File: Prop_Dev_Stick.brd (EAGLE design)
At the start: 63.2 x 24.9 mm, 54 parts, among them J1 MF-CON-MICROUSB-RIGHT, J3 M20-7822046, J4 M20-7822046, J5 M20-7820442, J6 M20-7820442, U1 P8X32A-Q44, U2 FT230XQ-R, U3 TPS2113ADRBR, U4 CAT24C512WI-GT3, U5 AD7999YRJZ-1500RL7, U6 TS2937CW33, U7 IRLML6401TRPBF, X1 ATS060CSM-1

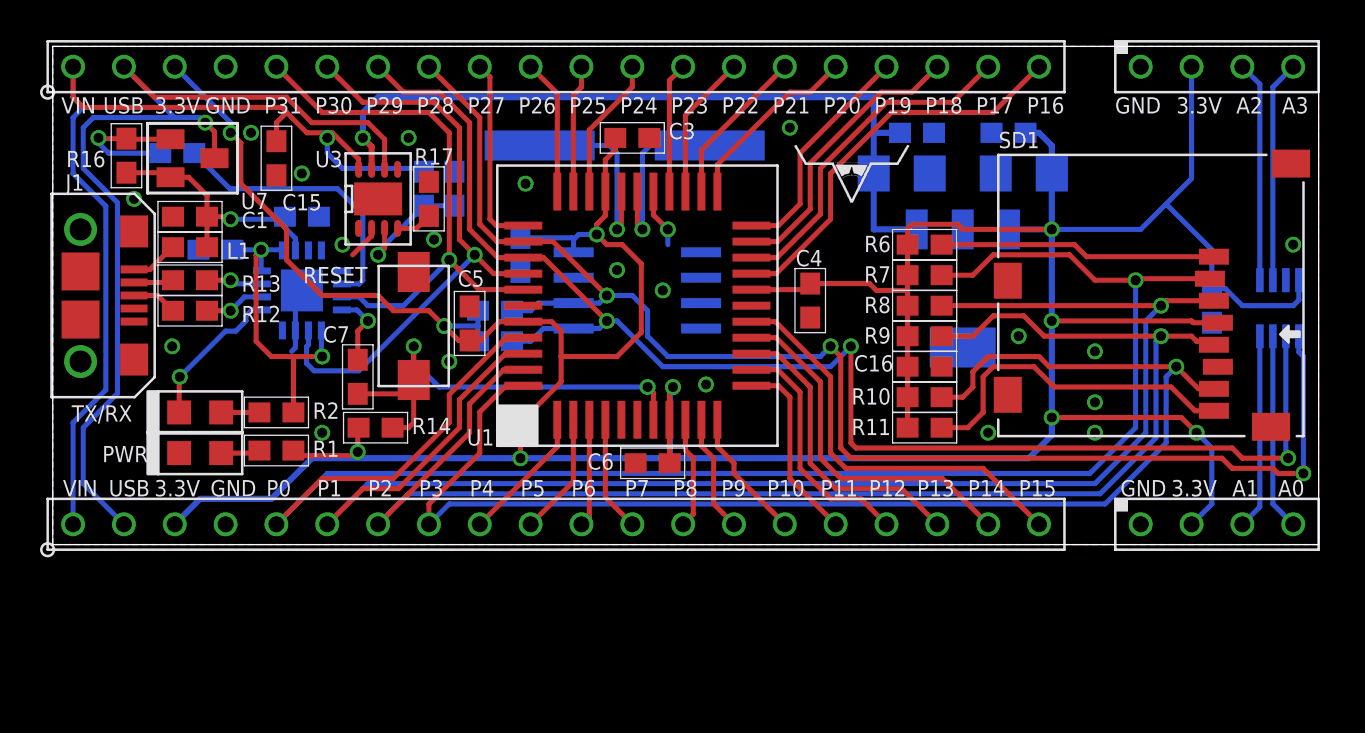
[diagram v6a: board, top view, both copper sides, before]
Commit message: Changed crystal.
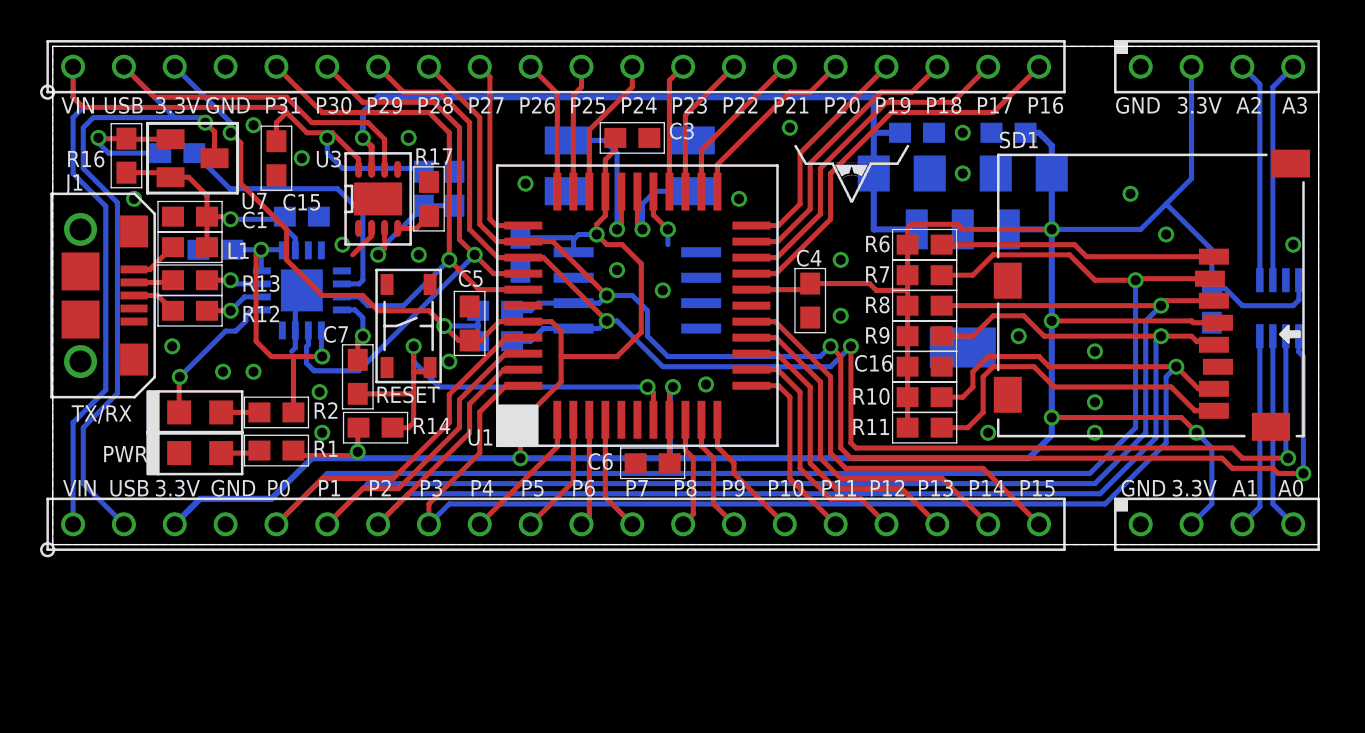
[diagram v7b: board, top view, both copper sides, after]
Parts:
- RESET: value 101-0134-EV -> MF-SW-TACT-4.2MM; device PP_Electromechanical:101-0134-EV -> MF_Switches:TACT4.2MM
- X1: value ATS060CSM-1 -> ABMM-6.000MHZ-B2-T; device PP_FreqCtrl:HC-49/US_SM -> MF_Frequency_Control:7MMX5MM
- moved X1 1.05 mm to (28.8, 18.9), turned to 0 degrees
- moved RESET 0.25 mm to (17.8, 10.9)
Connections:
- net GND: now also RESET.P$3, RESET.P$4, X1.P$2, X1.P$4; no longer RESET.1
- net RES: now also RESET.P$2; no longer RESET.2
- net X0: now also X1.P$3; no longer X1.P$1
- net X1: now also X1.P$1; no longer X1.P$2
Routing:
- net X1: track 9.32 -> 6.04 mm
- net X0: track 9.82 -> 8.57 mm
- net RES: track 22.8 -> 23.5 mm
- net GND: vias 21 -> 31
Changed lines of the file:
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@@
 <attribute name="DRAWING_NAME" x="62.738" y="19.05" size="0.8128" layer="22" font="vector" rot="MR0"/>
-</element>
-<element name="X1" library="PP_FreqCtrl" package="HC-49/US_SM" value="ATS060CSM-1" x="28.575" y="19.939" smashed="yes" rot="MR180">
-<attribute name="NAME" x="34.417" y="18.415" size="0.8128" layer="22" font="vector" rot="MR180"/>
 </element>
 <element name="U2" library="PP_DigitalIC" package="QFN-16" value="FT230XQ-R" x="12.446" y="12.7" smashed="yes" rot="MR90">
@@
 <element name="C7" library="PP_Passives" package="0603" value=".1uF" x="15.24" y="8.382" smashed="yes" rot="R270">
 <attribute name="NAME" x="13.497" y="10.0965" size="0.8128" layer="25" font="vector"/>
-</element>
-<element name="RESET" library="PP_Electromechanical" package="101-0134-EV" value="101-0134-EV" x="18.034" y="10.922" smashed="yes" rot="R270">
-<attribute name="NAME" x="12.51" y="13.057" size="0.8128" layer="25" font="vector"/>
 </element>
 <element name="U4" library="PP_DigitalIC" package="SOIC-8_W" value="CAT24C512WI-GT3" x="29.21" y="12.7" smashed="yes" rot="MR270">
@@
 <element name="J1" library="MF_Connectors" package="MICROUSB-RIGHT" value="MF-CON-MICROUSB-RIGHT" x="2.794" y="12.446" smashed="yes" rot="R270">
 <attribute name="NAME" x="0.635" y="17.686" size="0.8128" layer="25" font="vector"/>
+</element>
+<element name="X1" library="MF_Frequency_Control" package="7MMX5MM" value="ABMM-6.000MHZ-B2-T" x="28.829" y="18.923" smashed="yes" rot="MR0">
+<attribute name="NAME" x="32.429" y="21.923" size="0.8128" layer="26" font="vector" rot="MR0"/>
+</element>
+<element name="RESET" library="MF_Switches" package="TACT4.2MM" value="MF-SW-TACT-4.2MM" x="17.78" y="10.922" smashed="yes" rot="R270">
+<attribute name="NAME" x="16.123" y="7.08" size="0.8128" layer="25" font="vector"/>
 </element>
 </elements>
@@
 <contactref element="C4" pad="1"/>
 <contactref element="C5" pad="1"/>
-<contactref element="RESET" pad="1"/>
 <contactref element="U4" pad="4"/>
 <contactref element="U4" pad="2"/>
@@
 <via x="17.78" y="20.32" extent="1-16" drill="0.5"/>
 <via x="14.478" y="14.986" extent="1-16" drill="0.5"/>
-<via x="9.906" y="20.574" extent="1-16" drill="0.5"/>
+<via x="10.033" y="20.955" extent="1-16" drill="0.5"/>
 <via x="13.462" y="5.588" extent="1-16" drill="0.5"/>
 <wire x1="12.121" y1="10.7" x2="12.121" y2="9.835" width="0.254" layer="16"/>
 <wire x1="12.121" y1="9.835" x2="11.938" y2="9.652" width="0.254" layer="16"/>
 <wire x1="12.121" y1="12.375" x2="12.121" y2="10.7" width="0.254" layer="16"/>
-<via x="12.446" y="18.542" extent="1-16" drill="0.5"/>
+<via x="12.446" y="19.304" extent="1-16" drill="0.5"/>
 <via x="46.736" y="5.588" extent="1-16" drill="0.5"/>
 <via x="61.976" y="14.986" extent="1-16" drill="0.5"/>
@@
 <contactref element="J1" pad="S3"/>
 <contactref element="J1" pad="S2"/>
-<via x="19.05" y="15.24" extent="1-16" drill="0.5"/>
+<via x="18.288" y="14.478" extent="1-16" drill="0.5"/>
 <via x="23.622" y="18.034" extent="1-16" drill="0.5"/>
 <via x="28.194" y="13.716" extent="1-16" drill="0.5"/>
@@
 <wire x1="15.931" y1="15.797" x2="15.931" y2="15.423" width="0.254" layer="1"/>
 <wire x1="15.931" y1="15.423" x2="14.986" y2="14.478" width="0.254" layer="1"/>
+<contactref element="X1" pad="P$4"/>
+<contactref element="X1" pad="P$2"/>
+<contactref element="RESET" pad="P$3"/>
+<contactref element="RESET" pad="P$4"/>
+<via x="13.335" y="7.62" extent="1-16" drill="0.5"/>
+<via x="39.37" y="14.224" extent="1-16" drill="0.5"/>
+<via x="39.37" y="11.43" extent="1-16" drill="0.5"/>
+<via x="34.29" y="17.272" extent="1-16" drill="0.5"/>
+<via x="45.466" y="20.574" extent="1-16" drill="0.5"/>
+<via x="45.466" y="18.542" extent="1-16" drill="0.5"/>
+<via x="53.848" y="17.526" extent="1-16" drill="0.5"/>
+<via x="55.626" y="15.494" extent="1-16" drill="0.5"/>
+<via x="8.509" y="8.636" extent="1-16" drill="0.5"/>
+<via x="10.033" y="8.636" extent="1-16" drill="0.5"/>
 </signal>
 <signal name="SDA">
@@
 <signal name="RES">
 <contactref element="U1" pad="7"/>
-<contactref element="RESET" pad="2"/>
 <contactref element="R14" pad="1"/>
 <contactref element="C7" pad="2"/>
@@
 <wire x1="18.034" y1="9.144" x2="18.034" y2="9.906" width="0.254" layer="16"/>
 <via x="18.034" y="9.906" extent="1-16" drill="0.5"/>
-<wire x1="18.034" y1="9.906" x2="18.034" y2="8.222" width="0.254" layer="1"/>
-<wire x1="18.034" y1="8.222" x2="17.344" y2="7.532" width="0.254" layer="1"/>
-<wire x1="17.344" y1="7.532" x2="15.24" y2="7.532" width="0.254" layer="1"/>
+<wire x1="18.034" y1="7.532" x2="15.24" y2="7.532" width="0.254" layer="1"/>
 <wire x1="16.979" y1="5.842" x2="17.78" y2="5.842" width="0.254" layer="1"/>
 <wire x1="17.78" y1="5.842" x2="18.034" y2="6.096" width="0.254" layer="1"/>
-<wire x1="18.034" y1="6.096" x2="18.034" y2="8.222" width="0.254" layer="1"/>
+<contactref element="RESET" pad="P$2"/>
+<wire x1="18.034" y1="8.636" x2="18.034" y2="9.906" width="0.254" layer="1"/>
+<wire x1="18.855" y1="8.847" x2="18.812" y2="8.636" width="0.254" layer="1"/>
+<wire x1="18.812" y1="8.636" x2="18.034" y2="8.636" width="0.254" layer="1"/>
+<wire x1="18.034" y1="6.096" x2="18.034" y2="7.532" width="0.254" layer="1"/>
+<wire x1="18.034" y1="7.532" x2="18.034" y2="8.636" width="0.254" layer="1"/>
 </signal>
 <signal name="3.3V">
@@
 <wire x1="11.684" y1="15.748" x2="11.684" y2="14.224" width="0.254" layer="1"/>
 <wire x1="11.684" y1="14.224" x2="13.462" y2="12.446" width="0.254" layer="1"/>
-<wire x1="13.462" y1="12.446" x2="16.256" y2="12.446" width="0.254" layer="1"/>
-<wire x1="16.256" y1="12.446" x2="17.018" y2="11.684" width="0.254" layer="1"/>
-<wire x1="17.018" y1="11.684" x2="18.796" y2="11.684" width="0.254" layer="1"/>
+<wire x1="13.462" y1="12.446" x2="15.494" y2="12.446" width="0.254" layer="1"/>
+<wire x1="15.494" y1="12.446" x2="16.256" y2="11.684" width="0.254" layer="1"/>
+<wire x1="16.256" y1="11.684" x2="18.796" y2="11.684" width="0.254" layer="1"/>
 <wire x1="18.796" y1="11.684" x2="19.558" y2="10.922" width="0.254" layer="1"/>
 <wire x1="57.912" y1="12.788" x2="57.912" y2="14.732" width="0.254" layer="16"/>
@@
 <signal name="X0">
 <contactref element="U1" pad="29"/>
-<contactref element="X1" pad="P$1"/>
 <wire x1="28.41" y1="17.638" x2="28.41" y2="15.964" width="0.254" layer="1"/>
 <wire x1="28.41" y1="15.964" x2="28.194" y2="15.748" width="0.254" layer="1"/>
 <via x="28.194" y="15.748" extent="1-16" drill="0.5"/>
 <wire x1="28.194" y1="15.748" x2="28.194" y2="19.558" width="0.254" layer="16"/>
-<wire x1="28.194" y1="19.558" x2="27.813" y2="19.939" width="0.254" layer="16"/>
-<wire x1="27.813" y1="19.939" x2="24.325" y2="19.939" width="0.254" layer="16"/>
+<wire x1="28.194" y1="19.558" x2="27.559" y2="20.193" width="0.254" layer="16"/>
+<contactref element="X1" pad="P$3"/>
+<wire x1="27.559" y1="20.193" x2="25.679" y2="20.193" width="0.254" layer="16"/>
 </signal>
 <signal name="X1">
 <contactref element="U1" pad="28"/>
-<contactref element="X1" pad="P$2"/>
 <wire x1="29.21" y1="17.638" x2="29.21" y2="16.002" width="0.254" layer="1"/>
 <wire x1="29.21" y1="16.002" x2="29.464" y2="15.748" width="0.254" layer="1"/>
 <via x="29.464" y="15.748" extent="1-16" drill="0.5"/>
-<wire x1="29.464" y1="15.748" x2="29.464" y2="19.558" width="0.254" layer="16"/>
-<wire x1="29.464" y1="19.558" x2="29.845" y2="19.939" width="0.254" layer="16"/>
-<wire x1="29.845" y1="19.939" x2="32.825" y2="19.939" width="0.254" layer="16"/>
+<contactref element="X1" pad="P$1"/>
+<wire x1="29.464" y1="15.748" x2="29.464" y2="17.018" width="0.254" layer="16"/>
+<wire x1="29.464" y1="17.018" x2="30.099" y2="17.653" width="0.254" layer="16"/>
+<wire x1="30.099" y1="17.653" x2="31.979" y2="17.653" width="0.254" layer="16"/>
 </signal>
 <signal name="VBUS">
@@
 <contactref element="U2" pad="16"/>
 <contactref element="C7" pad="1"/>
-<wire x1="14.446" y1="11.725" x2="15.199" y2="11.725" width="0.254" layer="16"/>
-<wire x1="15.199" y1="11.725" x2="15.748" y2="11.176" width="0.254" layer="16"/>
-<via x="15.748" y="11.176" extent="1-16" drill="0.5"/>
-<wire x1="15.748" y1="11.176" x2="15.24" y2="10.668" width="0.254" layer="1"/>
-<wire x1="15.24" y1="10.668" x2="15.24" y2="9.232" width="0.254" layer="1"/>
+<via x="15.494" y="10.414" extent="1-16" drill="0.5"/>
+<wire x1="15.494" y1="10.414" x2="15.24" y2="10.16" width="0.254" layer="1"/>
+<wire x1="15.24" y1="10.16" x2="15.24" y2="9.232" width="0.254" layer="1"/>
+<wire x1="15.494" y1="10.414" x2="15.494" y2="11.33571875" width="0.254" layer="16"/>
+<wire x1="15.494" y1="11.33571875" x2="15.10471875" y2="11.725" width="0.254" layer="16"/>
+<wire x1="15.10471875" y1="11.725" x2="14.446" y2="11.725" width="0.254" layer="16"/>
 </signal>
 <signal name="P7">

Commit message: REV 4 push
New SD Card, MAX ADC, added 10uF cap.
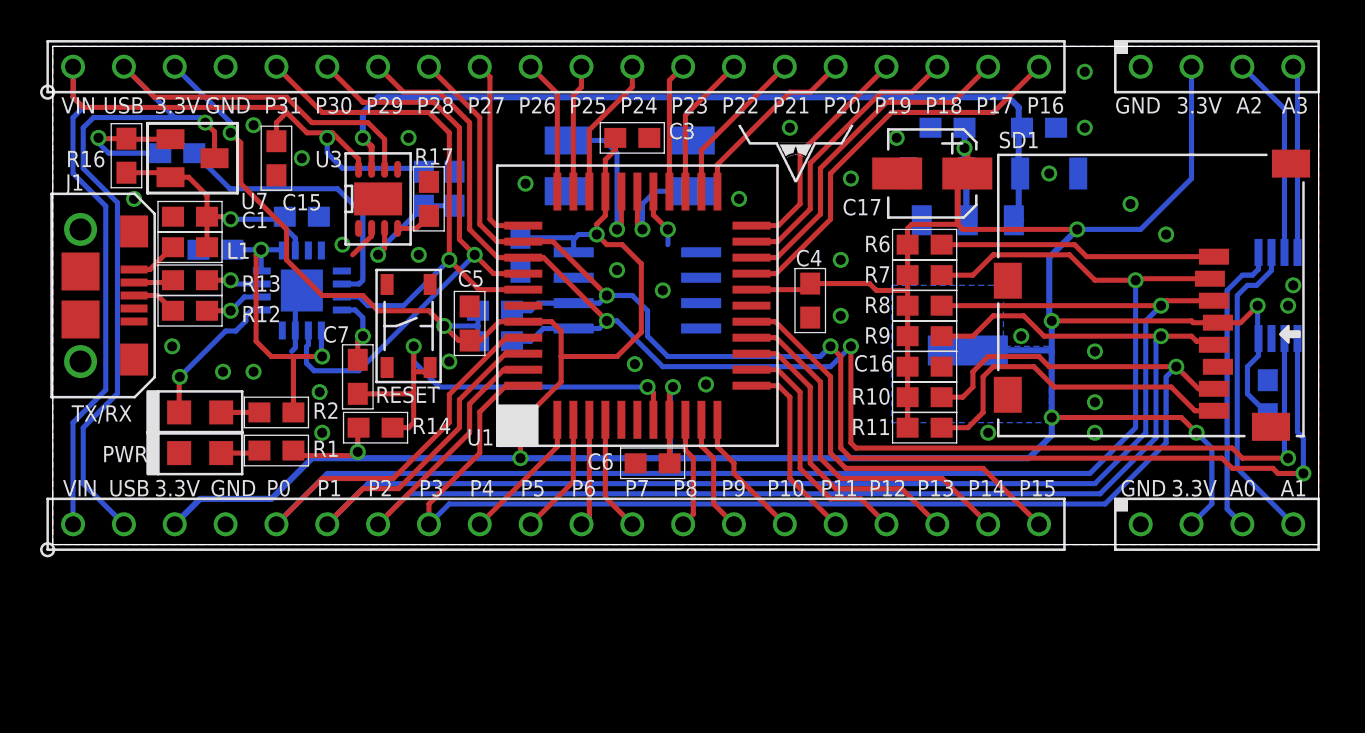
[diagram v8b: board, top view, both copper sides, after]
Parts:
- added C17: 10uF, MF_Passives:CP4MM
- C8, C9: device PP_Passives:1206 -> MF_Passives:C1206
- U5: value AD7999YRJZ-1500RL7 -> MAX11613EUA+; device PP_DigitalIC:SOT-23-8 -> PP_AnalogIC:UMAX-8
- U6: value TS2937CW33 -> NCP1117LPST33T3G; device PP_PowerIC:SOT-223 -> MF_IC_Power:SOT-223-3
- moved C10 6.10 mm to (49.3, 20.8)
- moved C14 5.36 mm to (60.7, 7.37), turned to 90 degrees
- moved C11 3.06 mm to (44.7, 20.8)
- moved U$2 2.97 mm to (39.1, 18.0)
- moved U6 2.81 mm to (45.7, 13.0)
- moved C9 1.78 mm to (44.2, 18.5), turned to 0 degrees
- moved C8 1.27 mm to (49.8, 18.5)
- moved U5 0.68 mm to (61.2, 12.4), turned to 270 degrees
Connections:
- net 3.3V: now also C17.P$1, C9.P$1, U5.P$8, U6.P$1, U6.P$3; no longer C8.1, U5.8, U6.OUT
- net 5V: now also C8.P$2, U6.P$4; no longer C9.1, U6.IN
- net A0: now also J6.3, U5.P$1; no longer J6.4, U5.3
- net A1: now also J6.4, U5.P$2; no longer J6.3, U5.4
- net A2: now also U5.P$3; no longer U5.5
- net A3: now also U5.P$4; no longer U5.6
- net GND: now also C17.P$2, C8.P$1, C9.P$2, U5.P$7, U6.P$2; no longer C8.2, C9.2, U5.7, U6.COM1, U6.COM2
- net SCL: now also U5.P$5; no longer U5.1
- net SDA: now also U5.P$6; no longer U5.2
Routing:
- net A1: track 9.76 -> 15.7 mm
- net A0: track 9.82 -> 14.8 mm
- net 5V: track 38.9 -> 43.0 mm
- net 3.3V: track 206.4 -> 209.7 mm, vias 10 -> 12
- net A3: track 11.1 -> 9.37 mm
- net A2: track 11.0 -> 10.2 mm
- net GND: vias 31 -> 36
- added copper zone on layer 16, net 3.3V
